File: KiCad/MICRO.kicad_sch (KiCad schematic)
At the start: 6 parts, among them U7 PIC32MX250F128D-IPT

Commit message: calefactor-Usart
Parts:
- added J2: DE9_Pins, symbol Connector:DE9_Pins
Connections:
- net SCL: now reaches U7.23 (RB2)
- net SDA: now reaches U7.24 (RB3)
- net RX: now reaches U7.43 (RB7)
- net RX: now also J2.2
- net TX: now reaches U7.9 (RB11)
- net TX: now also J2.3
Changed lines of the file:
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@@
+		)
+	)
+	(global_label "TX"
+		(shape input)
+		(at 123.19 92.71 180)
+		(fields_autoplaced yes)
+		(effects
+			(font
+				(size 1.27 1.27)
+			)
+			(justify right)
+		)
+		(property "Intersheetrefs" "${INTERSHEET_REFS}"
+			(at 118.0277 92.71 0)
+			(effects
+				(font
+					(size 1.27 1.27)
+				)
+				(justify right)
+				(hide yes)
+			)
+		)
+	)
+	(global_label "SDA"
+		(shape input)
+		(at 123.19 72.39 180)
+		(fields_autoplaced yes)
+		(effects
+			(font
+				(size 1.27 1.27)
+			)
+			(justify right)
+		)
+		(property "Intersheetrefs" "${INTERSHEET_REFS}"
+			(at 116.6367 72.39 0)
+			(effects
+				(font
+					(size 1.27 1.27)
+				)
+				(justify right)
+				(hide yes)
+			)
 		)
 	)
@@
 		)
 	)
+	(global_label "TX"
+		(shape input)
+		(at 220.98 88.9 180)
+		(fields_autoplaced yes)
+		(effects
+			(font
+				(size 1.27 1.27)
+			)
+			(justify right)
+		)
+		(property "Intersheetrefs" "${INTERSHEET_REFS}"
+			(at 215.8177 88.9 0)
+			(effects
+				(font
+					(size 1.27 1.27)
+				)
+				(justify right)
+				(hide yes)
+			)
+		)
+	)
 	(global_label "D"
 		(shape input)
@@
 		)
 	)
+	(global_label "SCL"
+		(shape input)
+		(at 123.19 69.85 180)
+		(fields_autoplaced yes)
+		(effects
+			(font
+				(size 1.27 1.27)
+			)
+			(justify right)
+		)
+		(property "Intersheetrefs" "${INTERSHEET_REFS}"
+			(at 116.6972 69.85 0)
+			(effects
+				(font
+					(size 1.27 1.27)
+				)
+				(justify right)
+				(hide yes)
+			)
+		)
+	)
 	(global_label "OSC1"
 		(shape input)
@@
 		)
 	)
+	(global_label "RX"
+		(shape input)
+		(at 123.19 82.55 180)
+		(fields_autoplaced yes)
+		(effects
+			(font
+				(size 1.27 1.27)
+			)
+			(justify right)
+		)
+		(property "Intersheetrefs" "${INTERSHEET_REFS}"
+			(at 117.7253 82.55 0)
+			(effects
+				(font
+					(size 1.27 1.27)
+				)
+				(justify right)
+				(hide yes)
+			)
+		)
+	)
+	(global_label "RX"
+		(shape input)
+		(at 220.98 93.98 180)
+		(fields_autoplaced yes)
+		(effects
+			(font
+				(size 1.27 1.27)
+			)
+			(justify right)
+		)
+		(property "Intersheetrefs" "${INTERSHEET_REFS}"
+			(at 215.5153 93.98 0)
+			(effects
+				(font
+					(size 1.27 1.27)
+				)
+				(justify right)
+				(hide yes)
+			)
+		)
+	)
 	(global_label "MCLR"
 		(shape input)
@@
 			)
 		)
+	)
+	(symbol
+		(lib_id "Connector:DE9_Pins")
+		(at 228.6 88.9 0)
+		(unit 1)
+		(exclude_from_sim no)
+		(in_bom yes)
+		(on_board yes)
+		(dnp no)
+		(fields_autoplaced yes)
+		(property "Reference" "J2"
+			(at 233.68 87.6299 0)
+			(effects
+				(font
+					(size 1.27 1.27)
+				)
+				(justify left)
+			)
+		)
+		(property "Value" "DE9_Pins"
+			(at 233.68 90.1699 0)
+			(effects
+				(font
+					(size 1.27 1.27)
+				)
+				(justify left)
+			)
+		)
+		(property "Footprint" ""
+			(at 228.6 88.9 0)
+			(effects
+				(font
+					(size 1.27 1.27)
+				)
+				(hide yes)
+			)
+		)
+		(property "Datasheet" "~"
+			(at 228.6 88.9 0)
+			(effects
+				(font
+					(size 1.27 1.27)
+				)
+				(hide yes)
+			)
+		)
+		(property "Description" "9-pin D-SUB connector, pins (male)"
+			(at 228.6 88.9 0)
+			(effects
+				(font
+					(size 1.27 1.27)
+				)
+				(hide yes)
+			)
+		)
+		(pin "4"
+		)
+		(pin "7"
+		)
+		(pin "1"
+		)
+		(pin "3"
+		)
+		(pin "2"
+		)
+		(pin "9"
+		)
+		(pin "8"
+		)
+		(pin "5"
+		)
+		(pin "6"
+		)
+		(instances
+			(project ""
+				(path "/9b9f005f-0621-4675-bd4e-683e7082b120/2f39354d-8df5-4269-96cb-5875be0a8958"
+					(reference "J2")
+					(unit 1)
+				)
+			)
+		)

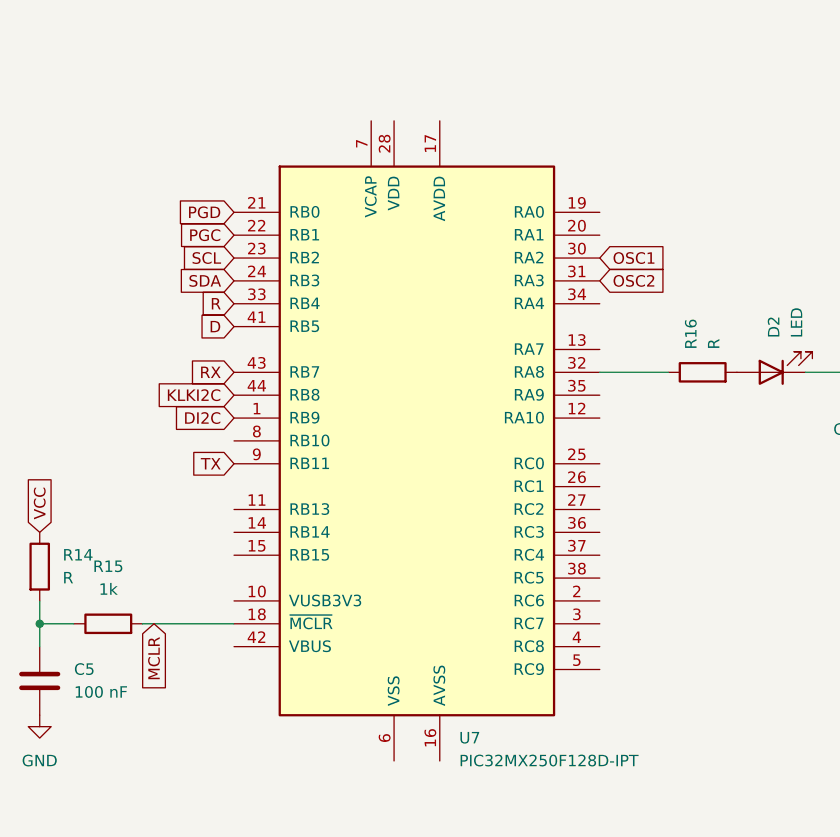
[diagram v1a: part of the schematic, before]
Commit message: añadido conexiones del PIC y cambiado lógica de los drivers para reducir pines
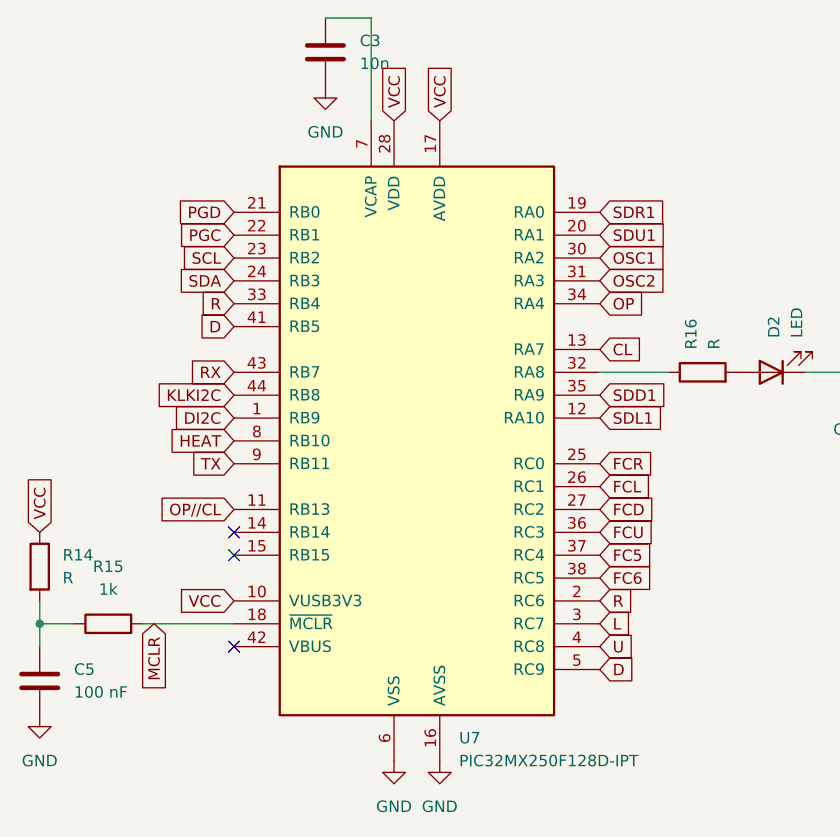
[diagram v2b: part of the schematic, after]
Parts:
- added C3: 10n, symbol Device:C
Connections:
- net D: now also U7.5 (RC9)
- net GND: now also U7.16 (AVSS), U7.29 (VSS), U7.39 (VSS), U7.6 (VSS), C3.2
- net R: now also U7.2 (RC6)
- net VCC: now also U7.10 (VUSB3V3), U7.17 (AVDD), U7.28 (VDD), U7.40 (VDD)
- net OP//CL: now reaches U7.11 (RB13)
- net SDL1: now reaches U7.12 (RA10)
- net CL: now reaches U7.13 (RA7)
- net SDR1: now reaches U7.19 (RA0)
- net SDU1: now reaches U7.20 (RA1)
- net FCR: now reaches U7.25 (RC0)
- net FCL: now reaches U7.26 (RC1)
- net FCD: now reaches U7.27 (RC2)
- net L: now reaches U7.3 (RC7)
- net OP: now reaches U7.34 (RA4)
- net SDD1: now reaches U7.35 (RA9)
- net FCU: now reaches U7.36 (RC3)
- net FC5: now reaches U7.37 (RC4)
- net FC6: now reaches U7.38 (RC5)
- net U: now reaches U7.4 (RC8)
- net at U7.7 (VCAP): now also C3.1
- net HEAT: now reaches U7.8 (RB10)
- no-connect marks 0 -> 3

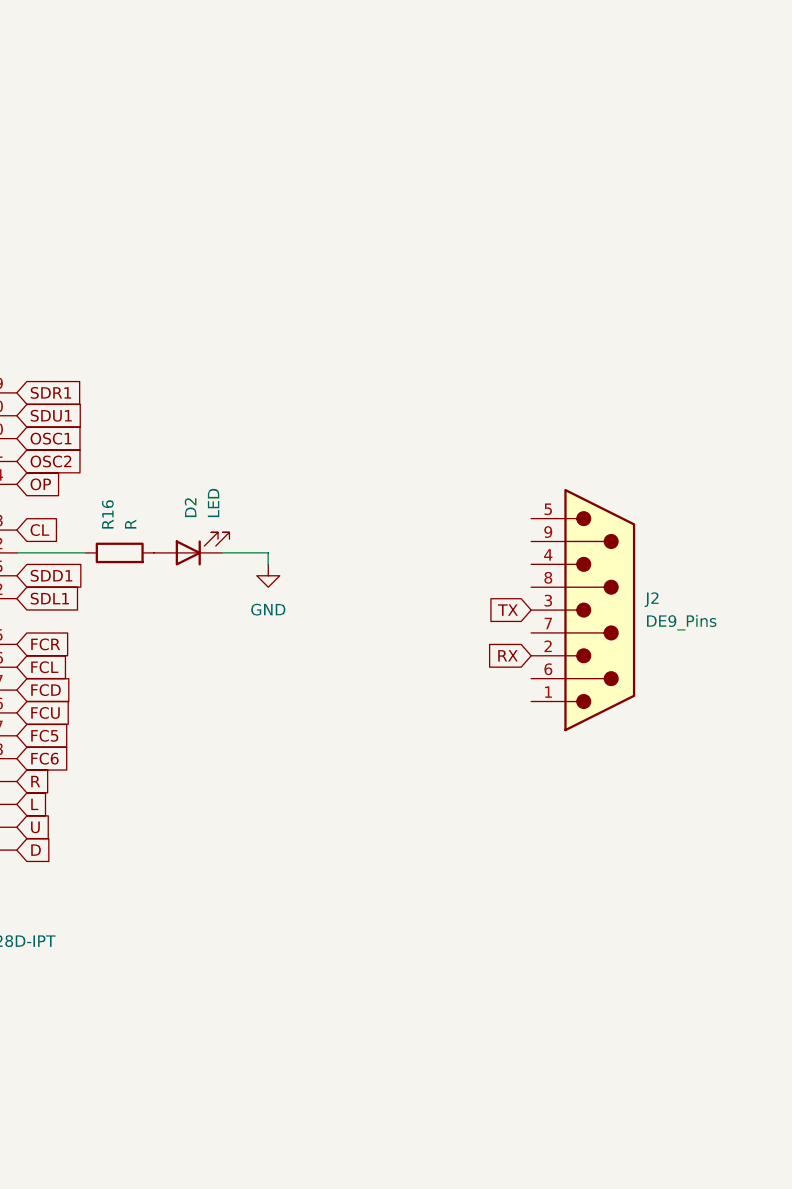
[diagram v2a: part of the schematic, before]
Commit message: canvis organització y reles calefactor
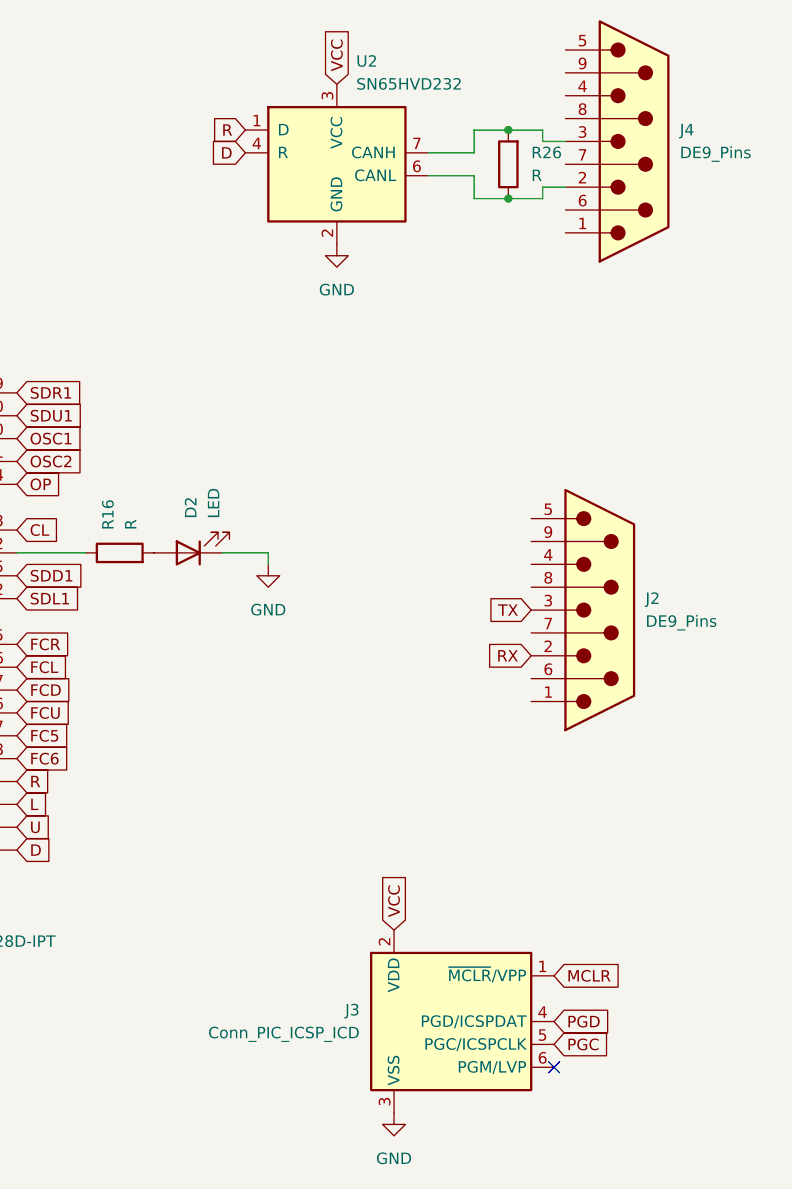
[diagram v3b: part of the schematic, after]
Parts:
- added J3: Conn_PIC_ICSP_ICD, symbol Connector:Conn_PIC_ICSP_ICD
- added J4: DE9_Pins, symbol Connector:DE9_Pins
- added R26: R, symbol Device:R
- added U2: SN65HVD232, Package_SO:SOIC-8_3.9x4.9mm_P1.27mm, symbol Interface_CAN_LIN:SN65HVD232
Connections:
- net D: now also U2.4 (R)
- net GND: now also J3.3 (VSS), U2.2 (GND)
- net MCLR: now also J3.1 (~{MCLR}/VPP)
- net PGC: now also J3.5 (PGC/ICSPCLK)
- net PGD: now also J3.4 (PGD/ICSPDAT)
- net R: now also U2.1 (D)
- net VCC: now also J3.2 (VDD), U2.3 (VCC)
- new net: J4.2, R26.1, U2.6 (CANL)
- new net: J4.3, R26.2, U2.7 (CANH)
- no-connect marks 3 -> 4

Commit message: he añadido huelas a algunos componentes importates
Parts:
- removed J3: Conn_PIC_ICSP_ICD, symbol Connector:Conn_PIC_ICSP_ICD
- added C6, C7: C, symbol Device:C
- added J8: Conn_PIC_ICSP_ICD, Connector_PinHeader_2.54mm:PinHeader_1x06_P2.54mm_Vertical, symbol Connector:Conn_PIC_ICSP_ICD
- added Y1: Crystal, Crystal:Crystal_HC49-4H_Vertical, symbol Device:Crystal
- J2, J4: footprint (none) -> Connector_Dsub:DSUB-9_Pins_Vertical_P2.77x2.84mm
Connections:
- net GND: now also C6.2, C7.2, J8.3 (VSS)
- net MCLR: now also J8.1 (~{MCLR}/VPP)
- net OSC1: now also C6.1, Y1.2
- net OSC2: now also C7.1, Y1.1
- net PGC: now also J8.5 (PGC/ICSPCLK)
- net PGD: now also J8.4 (PGD/ICSPDAT)
- net VCC: now also J8.2 (VDD)
- no-connect marks 4 -> 18
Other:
- moved on the sheet: J4, R26, U2

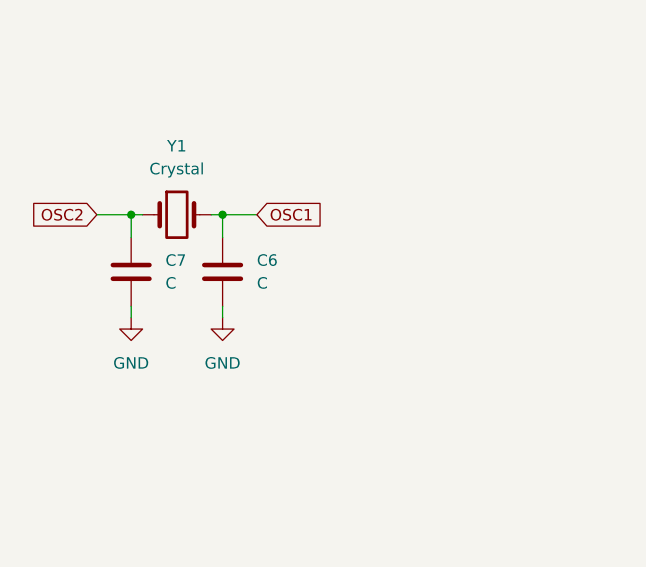
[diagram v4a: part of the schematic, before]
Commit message: he añadido el resto de huellas, he corregido algunos errores en la parte de alimentación en los diodos. tambien he trasladados todas las huellas a la pcb y lo he intentado separar un poco para verlo mas claro cuando empecemos el placing.
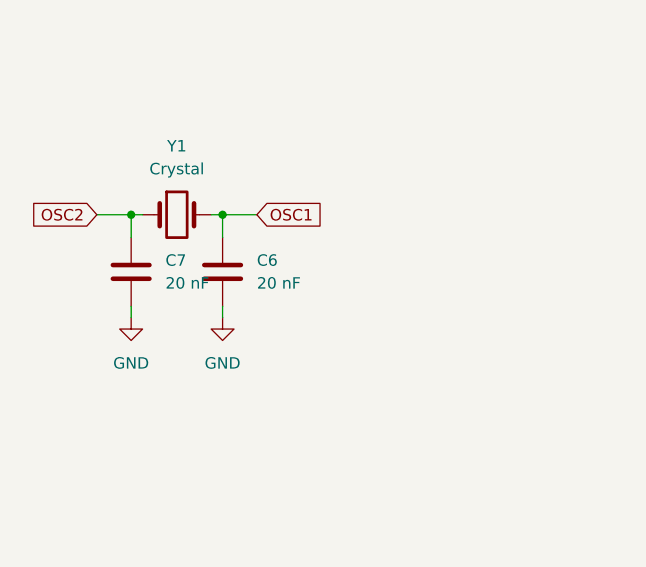
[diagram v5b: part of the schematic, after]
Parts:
- C3, C5: footprint (none) -> Capacitor_SMD:C_0402_1005Metric
- C6, C7: value C -> 20 nF; footprint (none) -> Capacitor_SMD:C_0402_1005Metric
- D2: footprint (none) -> LED_THT:LED_D3.0mm
- R14, R15, R26: footprint (none) -> Resistor_SMD:R_0402_1005Metric
- R16: footprint (none) -> Resistor_SMD:R_0805_2012Metric
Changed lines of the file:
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@@
 			)
 		)
-		(property "Footprint" ""
+		(property "Footprint" "Resistor_SMD:R_0402_1005Metric"
 			(at 243.078 43.18 90)
 			(effects
@@
 			)
 		)
-		(property "Footprint" ""
+		(property "Footprint" "Resistor_SMD:R_0402_1005Metric"
 			(at 99.822 104.14 90)
 			(effects
@@
 			)
 		)
-		(property "Value" "C"
+		(property "Value" "20 nF"
 			(at 62.23 59.6899 0)
 			(effects
@@
 			)
 		)
-		(property "Footprint" ""
+		(property "Footprint" "Capacitor_SMD:C_0402_1005Metric"
 			(at 59.3852 62.23 0)
 			(effects
@@
 			)
 		)
-		(property "Footprint" ""
+		(property "Footprint" "Resistor_SMD:R_0402_1005Metric"
 			(at 109.22 112.268 90)
 			(effects
@@
 			)
 		)
-		(property "Footprint" ""
+		(property "Footprint" "Resistor_SMD:R_0805_2012Metric"
 			(at 175.26 84.328 90)
 			(effects
@@
 			)
 		)
-		(property "Footprint" ""
+		(property "Footprint" "LED_THT:LED_D3.0mm"
 			(at 182.88 82.55 0)
 			(effects
@@
 			)
 		)
-		(property "Value" "C"
+		(property "Value" "20 nF"
 			(at 52.07 59.6899 0)
 			(effects
@@
 			)
 		)
-		(property "Footprint" ""
+		(property "Footprint" "Capacitor_SMD:C_0402_1005Metric"
 			(at 49.2252 62.23 0)
 			(effects
@@
 			)
 		)
-		(property "Footprint" ""
+		(property "Footprint" "Capacitor_SMD:C_0402_1005Metric"
 			(at 102.5652 120.65 0)
 			(effects
@@
 			)
 		)
-		(property "Footprint" ""
+		(property "Footprint" "Capacitor_SMD:C_0402_1005Metric"
 			(at 134.3152 50.8 0)
 			(effects

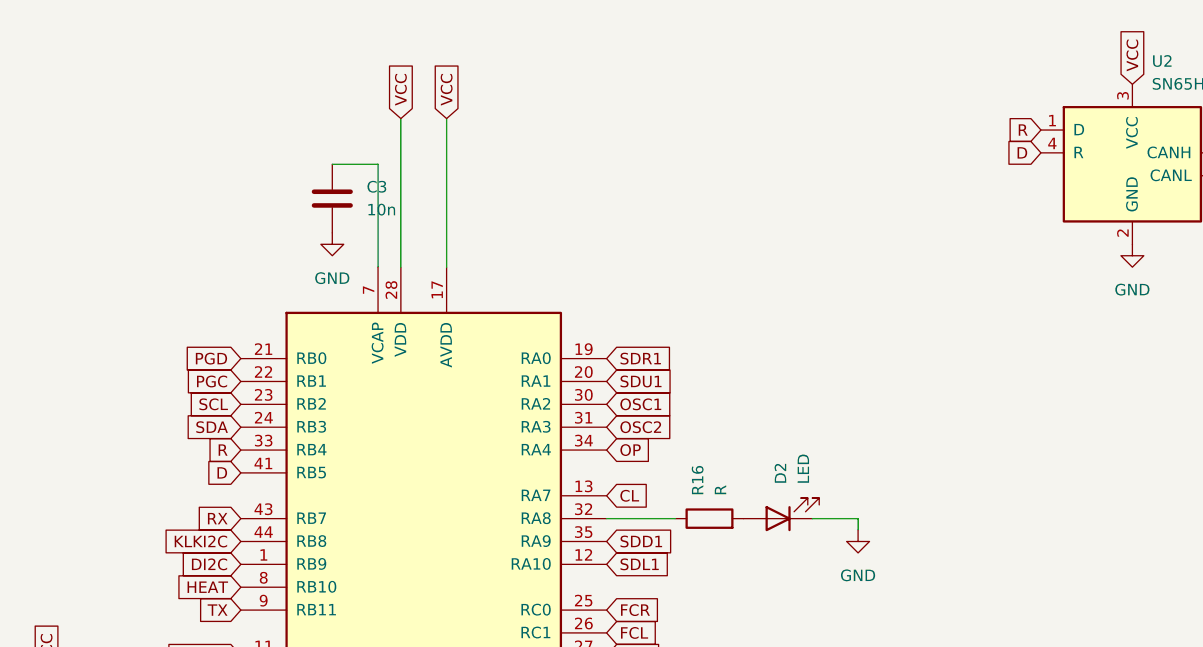
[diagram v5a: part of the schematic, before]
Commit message: he hecho el layout general menos el calefactor
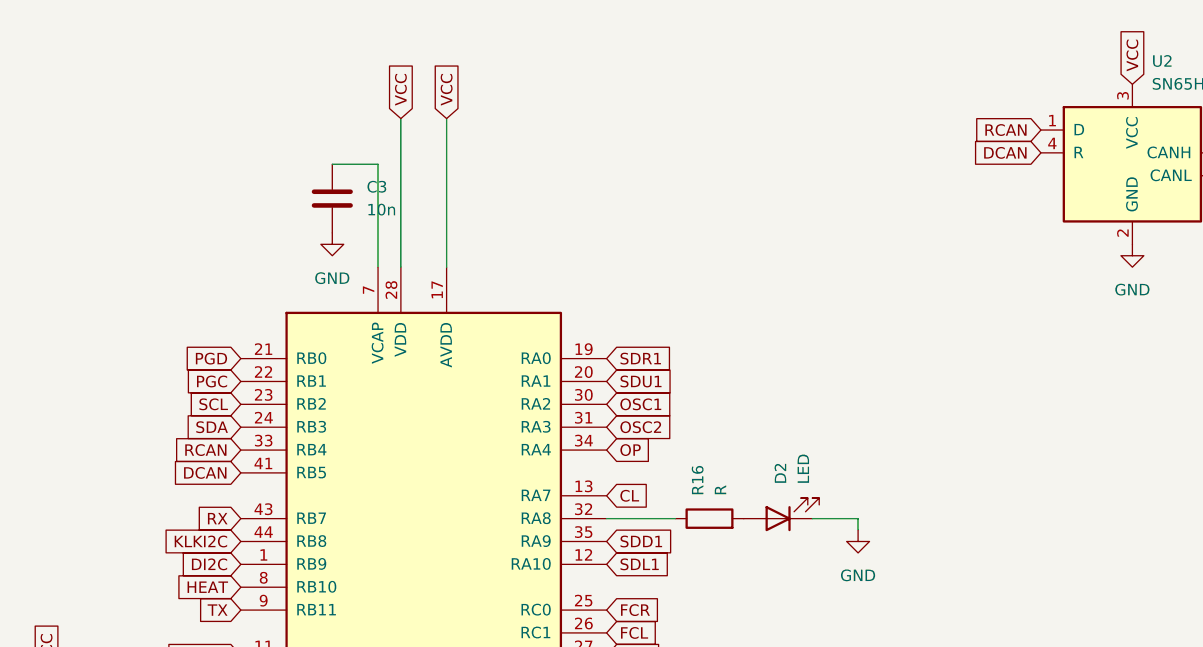
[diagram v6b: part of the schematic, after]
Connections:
- net D: no longer U2.4 (R), U7.41 (RB5)
- net R: no longer U2.1 (D), U7.33 (RB4)
- new net DCAN: U2.4 (R), U7.41 (RB5)
- new net RCAN: U2.1 (D), U7.33 (RB4)
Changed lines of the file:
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@@
 		)
 	)
-	(global_label "D"
+	(global_label "DCAN"
 		(shape input)
 		(at 212.09 41.91 180)
@@
 		)
 		(property "Intersheetrefs" "${INTERSHEET_REFS}"
-			(at 207.8348 41.91 0)
-			(effects
-				(font
-					(size 1.27 1.27)
-				)
-				(justify right)
-				(hide yes)
-			)
-		)
-	)
-	(global_label "R"
+			(at 204.1457 41.91 0)
+			(effects
+				(font
+					(size 1.27 1.27)
+				)
+				(justify right)
+				(hide yes)
+			)
+		)
+	)
+	(global_label "RCAN"
 		(shape input)
 		(at 212.09 39.37 180)
@@
 		)
 		(property "Intersheetrefs" "${INTERSHEET_REFS}"
-			(at 207.8348 39.37 0)
+			(at 204.1457 39.37 0)
 			(effects
 				(font
@@
 		)
 	)
-	(global_label "R"
+	(global_label "RCAN"
 		(shape input)
 		(at 123.19 74.93 180)
@@
 		)
 		(property "Intersheetrefs" "${INTERSHEET_REFS}"
-			(at 118.9348 74.93 0)
+			(at 115.2457 74.93 0)
 			(effects
 				(font
@@
 		)
 	)
-	(global_label "D"
+	(global_label "DCAN"
 		(shape input)
 		(at 123.19 77.47 180)
@@
 		)
 		(property "Intersheetrefs" "${INTERSHEET_REFS}"
-			(at 118.9348 77.47 0)
-			(effects
-				(font
+			(at 115.2457 77.47 0)
+			(effects
+				(font
